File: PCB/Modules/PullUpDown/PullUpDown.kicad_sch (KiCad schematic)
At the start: 3 parts

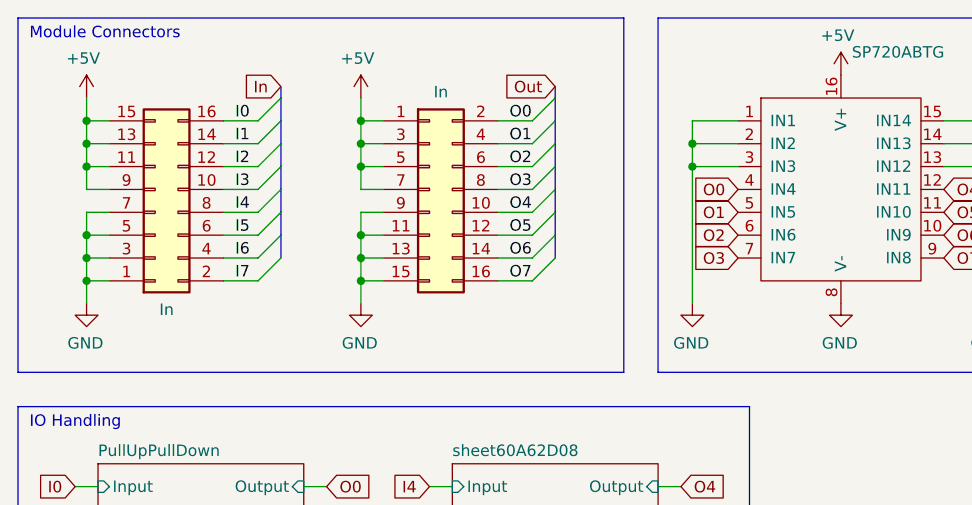
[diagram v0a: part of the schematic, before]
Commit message: Upgrade KiCad files from 6.0 to 7.0.
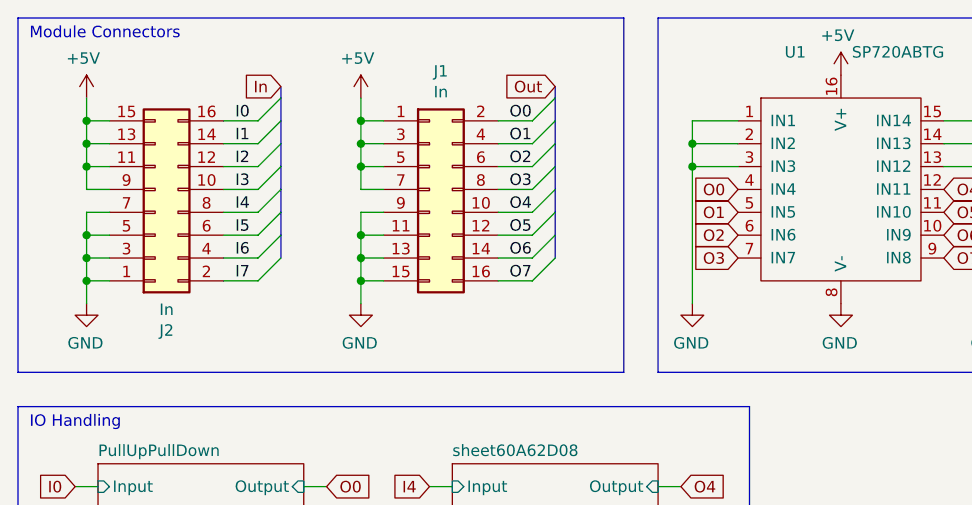
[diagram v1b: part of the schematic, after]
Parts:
- gave numbers to parts that had none: 3

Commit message: First pass of PCB rework.
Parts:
- J1: renamed from J2; footprint Custom:PinHeader_2x08_P2.54mm_Vertical-Centered -> KTANE:PinHeader_2x08_P2.54mm_Vertical-Centered
- J2: renamed from J1; footprint Custom:PinHeader_2x08_P2.54mm_Vertical-Centered -> KTANE:PinHeader_2x08_P2.54mm_Vertical-Centered
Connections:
- net +5V: no longer J1.11 (Pin_11), J1.13 (Pin_13), J1.9 (Pin_9), J2.1 (Pin_1), J2.3 (Pin_3), J2.5 (Pin_5), J2.7 (Pin_7), U1.16 (V+)
- net GND: no longer J1.3 (Pin_3), J1.5 (Pin_5), J1.7 (Pin_7), J2.11 (Pin_11), J2.13 (Pin_13), J2.15 (Pin_15), J2.9 (Pin_9)
- net I0: now also U1.4 (IN4)
- net I1: now also U1.5 (IN5)
- net I2: now also U1.6 (IN6)
- net I3: now also U1.7 (IN7)
- net I4: now also U1.12 (IN11)
- net I5: now also U1.11 (IN10)
- net I6: now also U1.10 (IN9)
- net I7: now also U1.9 (IN8)
- net O0: no longer U1.4 (IN4)
- net O1: no longer U1.5 (IN5)
- net O2: no longer U1.6 (IN6)
- net O3: no longer U1.7 (IN7)
- net O4: no longer U1.12 (IN11)
- net O5: no longer U1.11 (IN10)
- net O6: no longer U1.10 (IN9)
- net O7: no longer U1.9 (IN8)
- new net +3.3V: J1.13 (Pin_13), U1.16 (V+)
- new net I2C-CLK: J1.11 (Pin_11)
- new net I2C-DAT: J1.9 (Pin_9)
- new net LR1: J2.1 (Pin_1)
- new net LR2: J2.3 (Pin_3)
- new net LR3: J2.5 (Pin_5)
- new net LR4: J2.7 (Pin_7)
- new net LR5: J2.9 (Pin_9)
- new net LR6: J2.11 (Pin_11)
- new net LR7: J2.13 (Pin_13)
- new net LR8: J2.15 (Pin_15)
- new net SPI-CIPO: J1.3 (Pin_3)
- new net SPI-CLK: J1.7 (Pin_7)
- new net SPI-COPI: J1.5 (Pin_5)
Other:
- added sheet LowerRowSetting (lowerrow.kicad_sch)
- added sheet LowerRowSetting1 (lowerrow.kicad_sch)
- added sheet LowerRowSetting2 (lowerrow.kicad_sch)
- added sheet LowerRowSetting3 (lowerrow.kicad_sch)
- added sheet LowerRowSetting4 (lowerrow.kicad_sch)
- added sheet LowerRowSetting5 (lowerrow.kicad_sch)
- added sheet LowerRowSetting6 (lowerrow.kicad_sch)
- added sheet LowerRowSetting7 (lowerrow.kicad_sch)
- note added: "ESD"
- note added: "Lower Row Handling"
- moved on the sheet: J1, J2, U1

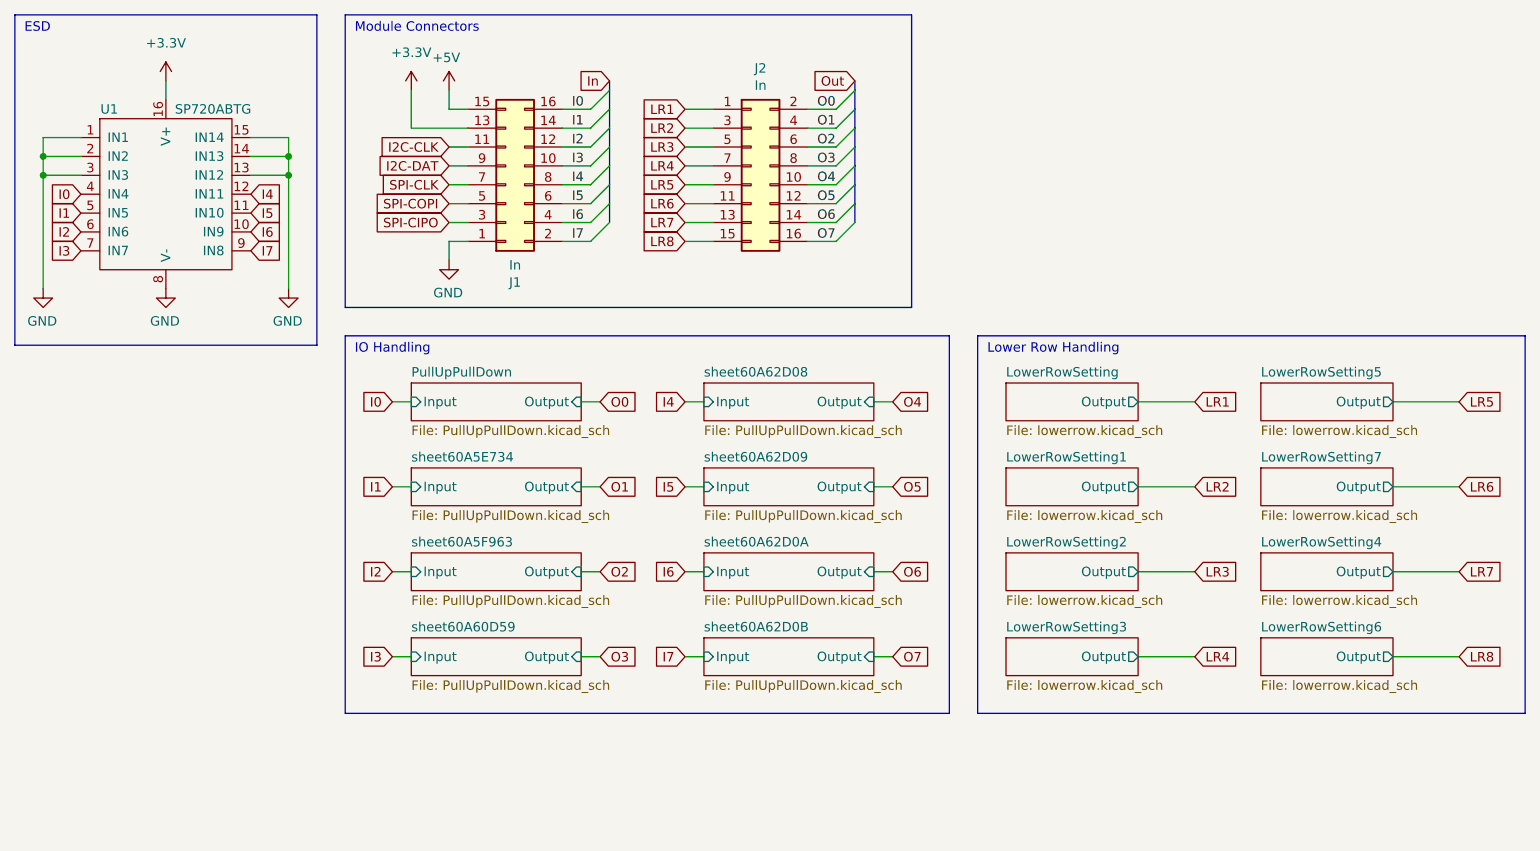
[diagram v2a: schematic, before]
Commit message: Update pull up/down module, with multivoltage ESD protection.
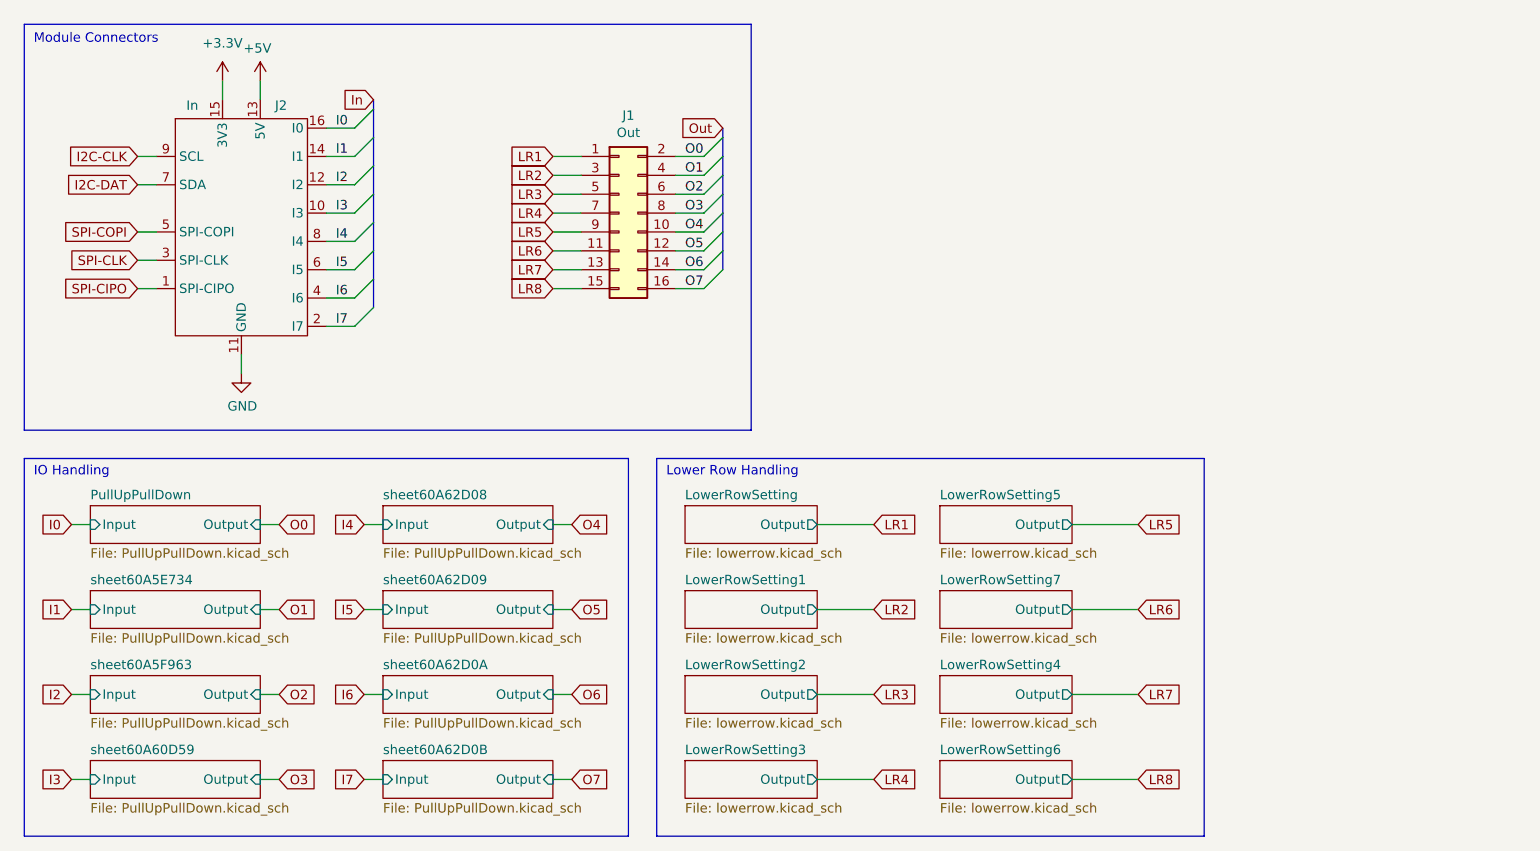
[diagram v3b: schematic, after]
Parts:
- removed J1: In, KTANE:PinHeader_2x08_P2.54mm_Vertical-Centered, symbol Connector_Generic:Conn_02x08_Odd_Even
- removed U1: SP720ABTG, Package_SO:SOIC-16_3.9x9.9mm_P1.27mm, symbol KTANE:SP720ABTG
- added J2: In, KTANE:KTANE Submodule Connector V2 - Short, symbol KTANE:Submodule
- J1: renamed from J2; value In -> Out; DIGIKEY (none) -> S9171-ND
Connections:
- net +3.3V: now also J2.15 (3V3)
- net +5V: now also J2.13 (5V)
- net GND: now also J2.11 (GND)
- net I0: now also J2.16 (I0)
- net I1: now also J2.14 (I1)
- net I2: now also J2.12 (I2)
- net I2C-CLK: now also J2.9 (SCL)
- net I2C-DAT: now also J2.7 (SDA)
- net I3: now also J2.10 (I3)
- net I4: now also J2.8 (I4)
- net I5: now also J2.6 (I5)
- net I6: now also J2.4 (I6)
- net I7: now also J2.2 (I7)
- net SPI-CIPO: now also J2.1 (SPI-CIPO)
- net SPI-CLK: now also J2.3 (SPI-CLK)
- net SPI-COPI: now also J2.5 (SPI-COPI)
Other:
- note removed: "ESD"
- moved on the sheet: J1
